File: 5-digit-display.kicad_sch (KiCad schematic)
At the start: 6 parts, among them U13 MAX7219, U14 3_digit_7_segment_display, U15 2_digit_7_segment_display

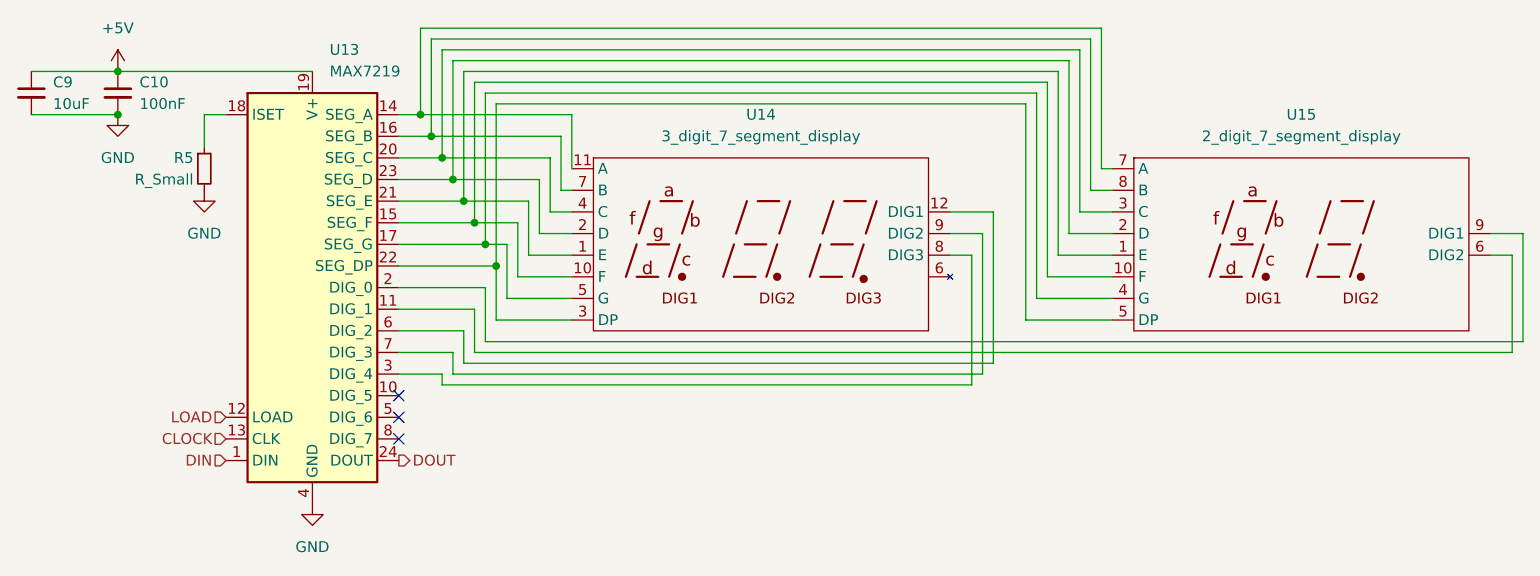
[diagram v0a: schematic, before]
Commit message: Add RP2040
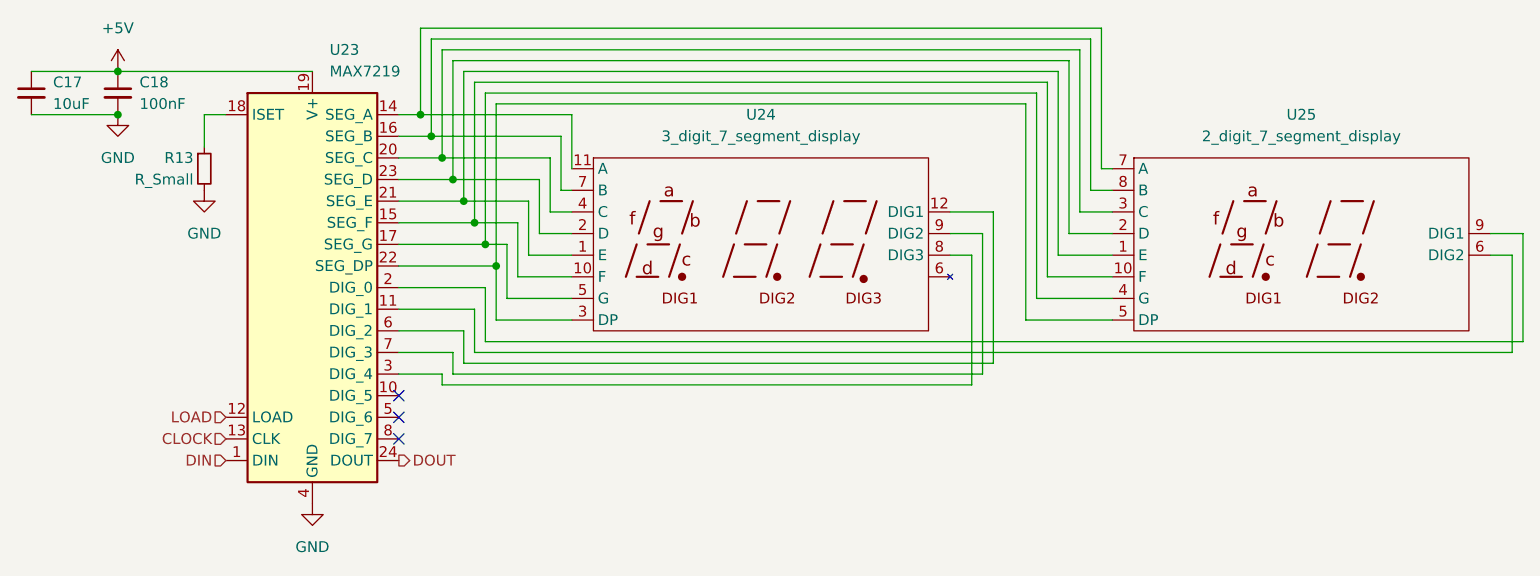
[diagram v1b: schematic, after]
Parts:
- renumbered C9 to C17, C10 to C18, R5 to R13, U13 to U23, U14 to U24, U15 to U25
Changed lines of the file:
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@@
   (symbol (lib_id "power:GND") (at 64.77 92.71 0)
     (in_bom yes) (on_board yes) (fields_autoplaced)
-    (property "Reference" "#PWR031" (id 0) (at 64.77 99.06 0)
+    (property "Reference" "#PWR040" (id 0) (at 64.77 99.06 0)
       (effects (font (size 1.27 1.27)) hide)
     )
@@
   (symbol (lib_id "Device:C_Small") (at 54.61 81.28 0)
     (in_bom yes) (on_board yes) (fields_autoplaced)
-    (property "Reference" "C10" (id 0) (at 57.15 80.0162 0)
+    (property "Reference" "C18" (id 0) (at 57.15 80.0162 0)
       (effects (font (size 1.27 1.27)) (justify left))
     )
@@
   (symbol (lib_id "Device:R_Small") (at 64.77 90.17 0)
     (in_bom yes) (on_board yes)
-    (property "Reference" "R5" (id 0) (at 63.5 88.9 0)
+    (property "Reference" "R13" (id 0) (at 63.5 88.9 0)
       (effects (font (size 1.27 1.27)) (justify right))
     )
@@
   (symbol (lib_id "Generic-radio-stack:2_digit_7_segment_display") (at 193.04 99.06 0)
     (in_bom yes) (on_board yes) (fields_autoplaced)
-    (property "Reference" "U15" (id 0) (at 193.675 83.82 0))
+    (property "Reference" "U25" (id 0) (at 193.675 83.82 0))
     (property "Value" "2_digit_7_segment_display" (id 1) (at 193.675 86.36 0))
     (property "Footprint" "" (id 2) (at 203.2 99.06 0)
@@
   (symbol (lib_id "power:GND") (at 77.47 129.54 0)
     (in_bom yes) (on_board yes) (fields_autoplaced)
-    (property "Reference" "#PWR032" (id 0) (at 77.47 135.89 0)
+    (property "Reference" "#PWR041" (id 0) (at 77.47 135.89 0)
       (effects (font (size 1.27 1.27)) hide)
     )
@@
   (symbol (lib_id "Driver_LED:MAX7219") (at 77.47 104.14 0)
     (in_bom yes) (on_board yes) (fields_autoplaced)
-    (property "Reference" "U13" (id 0) (at 79.4894 76.2 0)
+    (property "Reference" "U23" (id 0) (at 79.4894 76.2 0)
       (effects (font (size 1.27 1.27)) (justify left))
     )
@@
   (symbol (lib_id "Generic-radio-stack:3_digit_7_segment_display") (at 129.54 99.06 0)
     (in_bom yes) (on_board yes) (fields_autoplaced)
-    (property "Reference" "U14" (id 0) (at 130.175 83.82 0))
+    (property "Reference" "U24" (id 0) (at 130.175 83.82 0))
     (property "Value" "3_digit_7_segment_display" (id 1) (at 130.175 86.36 0))
     (property "Footprint" "" (id 2) (at 134.62 99.06 0)
@@
   (symbol (lib_id "power:GND") (at 54.61 83.82 0)
     (in_bom yes) (on_board yes) (fields_autoplaced)
-    (property "Reference" "#PWR030" (id 0) (at 54.61 90.17 0)
+    (property "Reference" "#PWR039" (id 0) (at 54.61 90.17 0)
       (effects (font (size 1.27 1.27)) hide)
     )
@@
   (symbol (lib_id "power:+5V") (at 54.61 78.74 0)
     (in_bom yes) (on_board yes) (fields_autoplaced)
-    (property "Reference" "#PWR029" (id 0) (at 54.61 82.55 0)
+    (property "Reference" "#PWR038" (id 0) (at 54.61 82.55 0)
       (effects (font (size 1.27 1.27)) hide)
     )
@@
   (symbol (lib_id "Device:C_Small") (at 44.45 81.28 0)
     (in_bom yes) (on_board yes) (fields_autoplaced)
-    (property "Reference" "C9" (id 0) (at 46.99 80.0162 0)
+    (property "Reference" "C17" (id 0) (at 46.99 80.0162 0)
       (effects (font (size 1.27 1.27)) (justify left))
     )

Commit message: Bunch more schematic work
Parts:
- C18: footprint (none) -> Capacitor_SMD:C_0805_2012Metric
- R17: renamed from R13; footprint (none) -> Resistor_SMD:R_0805_2012Metric
- U23: footprint (none) -> Package_SO:SOIC-24W_7.5x15.4mm_P1.27mm
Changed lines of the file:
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@@
   (symbol (lib_id "power:GND") (at 64.77 92.71 0)
     (in_bom yes) (on_board yes) (fields_autoplaced)
-    (property "Reference" "#PWR040" (id 0) (at 64.77 99.06 0)
+    (property "Reference" "#PWR042" (id 0) (at 64.77 99.06 0)
       (effects (font (size 1.27 1.27)) hide)
     )
@@
       (effects (font (size 1.27 1.27)) (justify left))
     )
-    (property "Footprint" "" (id 2) (at 54.61 81.28 0)
+    (property "Footprint" "Capacitor_SMD:C_0805_2012Metric" (id 2) (at 54.61 81.28 0)
       (effects (font (size 1.27 1.27)) hide)
     )
@@
   (symbol (lib_id "Device:R_Small") (at 64.77 90.17 0)
     (in_bom yes) (on_board yes)
-    (property "Reference" "R13" (id 0) (at 63.5 88.9 0)
+    (property "Reference" "R17" (id 0) (at 63.5 88.9 0)
       (effects (font (size 1.27 1.27)) (justify right))
     )
@@
       (effects (font (size 1.27 1.27)) (justify right))
     )
-    (property "Footprint" "" (id 2) (at 64.77 90.17 0)
+    (property "Footprint" "Resistor_SMD:R_0805_2012Metric" (id 2) (at 64.77 90.17 0)
       (effects (font (size 1.27 1.27)) hide)
     )
@@
   (symbol (lib_id "power:GND") (at 77.47 129.54 0)
     (in_bom yes) (on_board yes) (fields_autoplaced)
-    (property "Reference" "#PWR041" (id 0) (at 77.47 135.89 0)
+    (property "Reference" "#PWR043" (id 0) (at 77.47 135.89 0)
       (effects (font (size 1.27 1.27)) hide)
     )
@@
       (effects (font (size 1.27 1.27)) (justify left))
     )
-    (property "Footprint" "" (id 2) (at 76.2 102.87 0)
+    (property "Footprint" "Package_SO:SOIC-24W_7.5x15.4mm_P1.27mm" (id 2) (at 76.2 102.87 0)
       (effects (font (size 1.27 1.27)) hide)
     )
@@
   (symbol (lib_id "power:GND") (at 54.61 83.82 0)
     (in_bom yes) (on_board yes) (fields_autoplaced)
-    (property "Reference" "#PWR039" (id 0) (at 54.61 90.17 0)
+    (property "Reference" "#PWR041" (id 0) (at 54.61 90.17 0)
       (effects (font (size 1.27 1.27)) hide)
     )
@@
   (symbol (lib_id "power:+5V") (at 54.61 78.74 0)
     (in_bom yes) (on_board yes) (fields_autoplaced)
-    (property "Reference" "#PWR038" (id 0) (at 54.61 82.55 0)
+    (property "Reference" "#PWR040" (id 0) (at 54.61 82.55 0)
       (effects (font (size 1.27 1.27)) hide)
     )

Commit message: Add display footprints and models
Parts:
- C17: footprint (none) -> Generic-radio-stack:Perfect_0402
- C18: footprint Capacitor_SMD:C_0805_2012Metric -> Generic-radio-stack:Perfect_0402
- R17: footprint Resistor_SMD:R_0805_2012Metric -> Generic-radio-stack:Perfect_0402
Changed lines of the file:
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@@
       (effects (font (size 1.27 1.27)) (justify left))
     )
-    (property "Footprint" "Capacitor_SMD:C_0805_2012Metric" (id 2) (at 54.61 81.28 0)
+    (property "Footprint" "Generic-radio-stack:Perfect_0402" (id 2) (at 54.61 81.28 0)
       (effects (font (size 1.27 1.27)) hide)
     )
@@
       (effects (font (size 1.27 1.27)) (justify right))
     )
-    (property "Footprint" "Resistor_SMD:R_0805_2012Metric" (id 2) (at 64.77 90.17 0)
+    (property "Footprint" "Generic-radio-stack:Perfect_0402" (id 2) (at 64.77 90.17 0)
       (effects (font (size 1.27 1.27)) hide)
     )
@@
       (effects (font (size 1.27 1.27)) (justify left))
     )
-    (property "Footprint" "" (id 2) (at 44.45 81.28 0)
+    (property "Footprint" "Generic-radio-stack:Perfect_0402" (id 2) (at 44.45 81.28 0)
       (effects (font (size 1.27 1.27)) hide)
     )

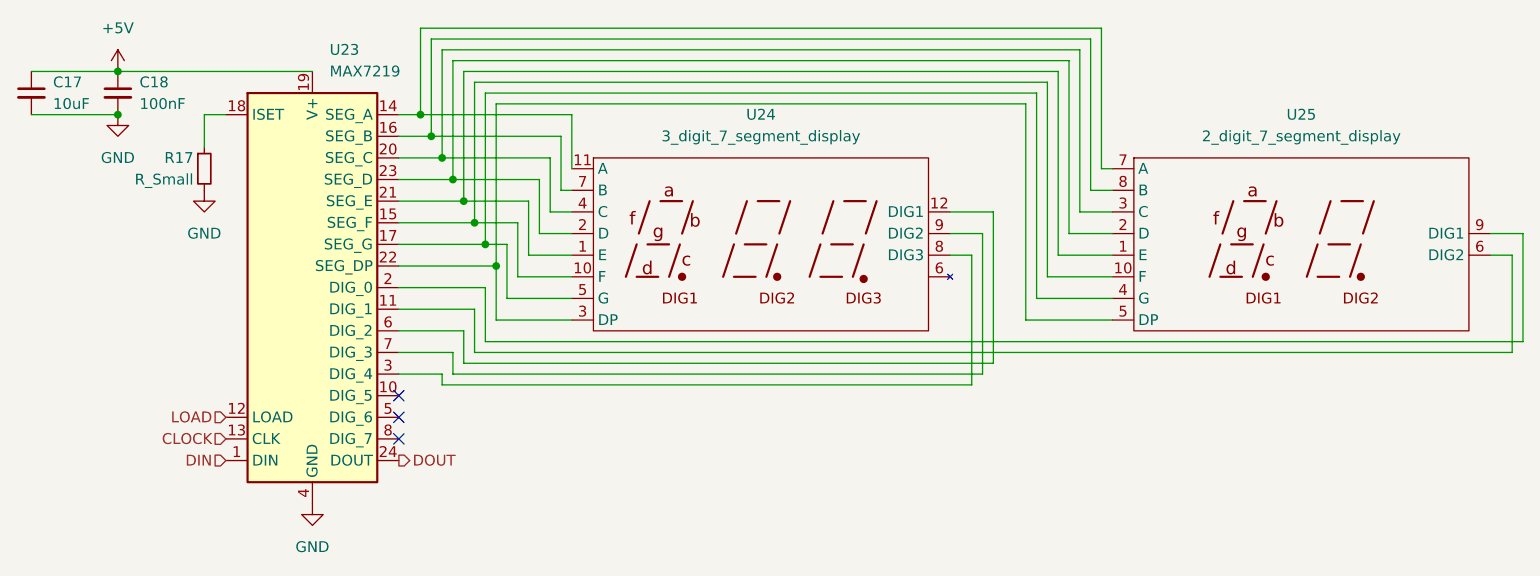
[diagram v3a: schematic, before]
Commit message: Custom component for six digit display
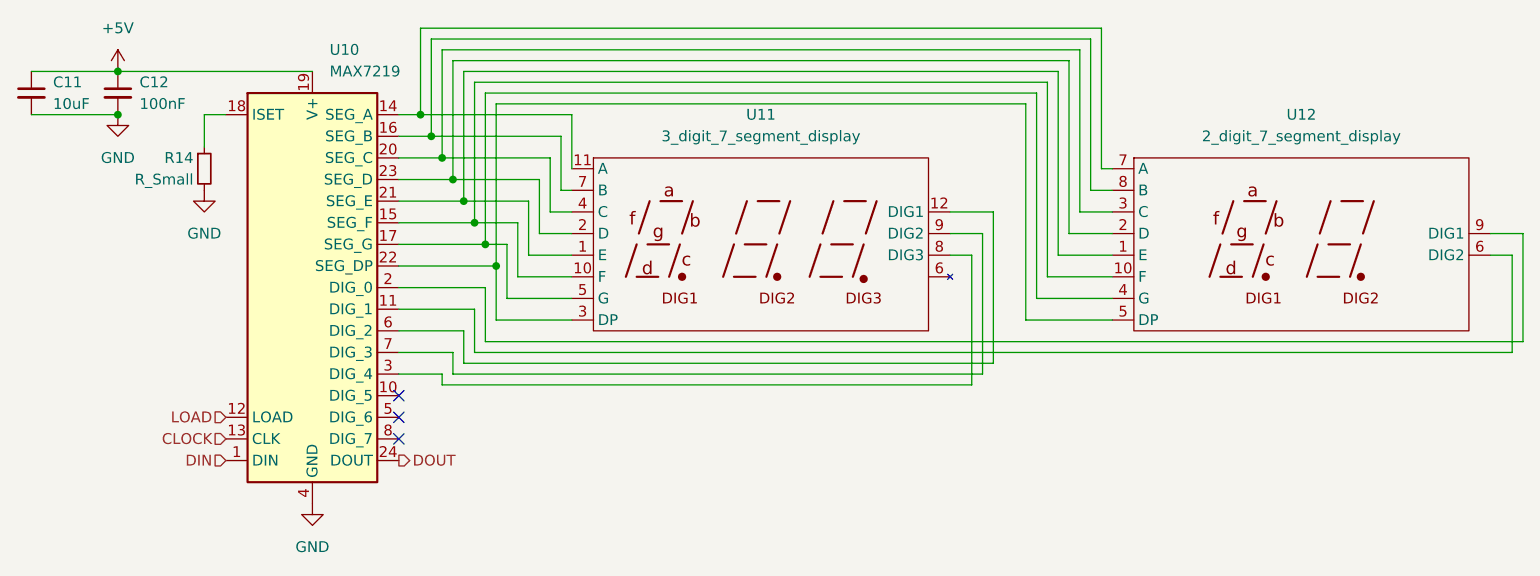
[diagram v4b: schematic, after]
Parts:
- U11: renamed from U24; footprint (none) -> Generic-radio-stack:3_digit_7_segment_LED
- U12: renamed from U25; footprint (none) -> Generic-radio-stack:2_digit_7_segment_LED
- renumbered C17 to C11, C18 to C12, R17 to R14, U23 to U10
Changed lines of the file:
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@@
   (symbol (lib_id "Device:C_Small") (at 54.61 81.28 0)
     (in_bom yes) (on_board yes) (fields_autoplaced)
-    (property "Reference" "C18" (id 0) (at 57.15 80.0162 0)
+    (property "Reference" "C12" (id 0) (at 57.15 80.0162 0)
       (effects (font (size 1.27 1.27)) (justify left))
     )
@@
   (symbol (lib_id "Device:R_Small") (at 64.77 90.17 0)
     (in_bom yes) (on_board yes)
-    (property "Reference" "R17" (id 0) (at 63.5 88.9 0)
+    (property "Reference" "R14" (id 0) (at 63.5 88.9 0)
       (effects (font (size 1.27 1.27)) (justify right))
     )
@@
   (symbol (lib_id "Generic-radio-stack:2_digit_7_segment_display") (at 193.04 99.06 0)
     (in_bom yes) (on_board yes) (fields_autoplaced)
-    (property "Reference" "U25" (id 0) (at 193.675 83.82 0))
+    (property "Reference" "U12" (id 0) (at 193.675 83.82 0))
     (property "Value" "2_digit_7_segment_display" (id 1) (at 193.675 86.36 0))
-    (property "Footprint" "" (id 2) (at 203.2 99.06 0)
+    (property "Footprint" "Generic-radio-stack:2_digit_7_segment_LED" (id 2) (at 203.2 99.06 0)
       (effects (font (size 1.27 1.27)) hide)
     )
@@
   (symbol (lib_id "Driver_LED:MAX7219") (at 77.47 104.14 0)
     (in_bom yes) (on_board yes) (fields_autoplaced)
-    (property "Reference" "U23" (id 0) (at 79.4894 76.2 0)
+    (property "Reference" "U10" (id 0) (at 79.4894 76.2 0)
       (effects (font (size 1.27 1.27)) (justify left))
     )
@@
   (symbol (lib_id "Generic-radio-stack:3_digit_7_segment_display") (at 129.54 99.06 0)
     (in_bom yes) (on_board yes) (fields_autoplaced)
-    (property "Reference" "U24" (id 0) (at 130.175 83.82 0))
+    (property "Reference" "U11" (id 0) (at 130.175 83.82 0))
     (property "Value" "3_digit_7_segment_display" (id 1) (at 130.175 86.36 0))
-    (property "Footprint" "" (id 2) (at 134.62 99.06 0)
+    (property "Footprint" "Generic-radio-stack:3_digit_7_segment_LED" (id 2) (at 134.62 99.06 0)
       (effects (font (size 1.27 1.27)) hide)
     )
@@
   (symbol (lib_id "Device:C_Small") (at 44.45 81.28 0)
     (in_bom yes) (on_board yes) (fields_autoplaced)
-    (property "Reference" "C17" (id 0) (at 46.99 80.0162 0)
+    (property "Reference" "C11" (id 0) (at 46.99 80.0162 0)
       (effects (font (size 1.27 1.27)) (justify left))
     )

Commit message: More footprint updates
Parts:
- removed U11: 3_digit_7_segment_display, Generic-radio-stack:3_digit_7_segment_LED, symbol Generic-radio-stack:3_digit_7_segment_display
- removed U12: 2_digit_7_segment_display, Generic-radio-stack:2_digit_7_segment_LED, symbol Generic-radio-stack:2_digit_7_segment_display
- added U11: 5_digit_7_segment_display, Generic-radio-stack:5 digit (3+2) 7 segment LED display, symbol Generic-radio-stack:5_digit_7_segment_display
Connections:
- net E: now reaches U10.21 (SEG_E)
- net E: now also U11.1 (E), U11.13 (E')
- net F: now reaches U10.15 (SEG_F)
- net F: now also U11.10 (F), U11.22 (F')
- net D: now reaches U10.23 (SEG_D)
- net D: now also U11.14 (D'), U11.2 (D)
- net C: now reaches U10.20 (SEG_C)
- net C: now also U11.15 (C'), U11.4 (C)
- net G: now reaches U10.17 (SEG_G)
- net G: now also U11.16 (G'), U11.5 (G)
- net DP: now reaches U10.22 (SEG_DP)
- net DP: now also U11.17 (DP'), U11.3 (DP)
- net DIG_1: now reaches U10.11 (DIG_1)
- net DIG_1: now also U11.21 (DIG1')
- net A: now reaches U10.14 (SEG_A)
- net A: now also U11.11 (A), U11.19 (A')
- net B: now reaches U10.16 (SEG_B)
- net B: now also U11.20 (B'), U11.7 (B)
- net DIG_0: now reaches U10.2 (DIG_0)
- net DIG_0: now also U11.18 (DIG2')
- net DIG_4: now reaches U10.3 (DIG_4)
- net DIG_4: now also U11.12 (DIG1)
- net DIG_2: now reaches U10.6 (DIG_2)
- net DIG_2: now also U11.8 (DIG3)
- net DIG_3: now reaches U10.7 (DIG_3)
- net DIG_3: now also U11.9 (DIG2)

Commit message: Board layout begins. Ugh.
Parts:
- renumbered C11 to C17, C12 to C18, R14 to R17, U10 to U16, U11 to U17
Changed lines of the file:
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@@
   (symbol (lib_id "power:GND") (at 64.77 92.71 0)
     (in_bom yes) (on_board yes) (fields_autoplaced)
-    (property "Reference" "#PWR030" (id 0) (at 64.77 99.06 0)
+    (property "Reference" "#PWR042" (id 0) (at 64.77 99.06 0)
       (effects (font (size 1.27 1.27)) hide)
     )
@@
   (symbol (lib_id "Device:C_Small") (at 54.61 81.28 0)
     (in_bom yes) (on_board yes) (fields_autoplaced)
-    (property "Reference" "C12" (id 0) (at 57.15 80.0162 0)
+    (property "Reference" "C18" (id 0) (at 57.15 80.0162 0)
       (effects (font (size 1.27 1.27)) (justify left))
     )
@@
   (symbol (lib_id "Device:R_Small") (at 64.77 90.17 0)
     (in_bom yes) (on_board yes)
-    (property "Reference" "R14" (id 0) (at 63.5 88.9 0)
+    (property "Reference" "R17" (id 0) (at 63.5 88.9 0)
       (effects (font (size 1.27 1.27)) (justify right))
     )
@@
   (symbol (lib_id "power:GND") (at 77.47 129.54 0)
     (in_bom yes) (on_board yes) (fields_autoplaced)
-    (property "Reference" "#PWR031" (id 0) (at 77.47 135.89 0)
+    (property "Reference" "#PWR043" (id 0) (at 77.47 135.89 0)
       (effects (font (size 1.27 1.27)) hide)
     )
@@
   (symbol (lib_id "Driver_LED:MAX7219") (at 77.47 104.14 0)
     (in_bom yes) (on_board yes) (fields_autoplaced)
-    (property "Reference" "U10" (id 0) (at 79.4894 76.2 0)
+    (property "Reference" "U16" (id 0) (at 79.4894 76.2 0)
       (effects (font (size 1.27 1.27)) (justify left))
     )
@@
   (symbol (lib_id "power:GND") (at 54.61 83.82 0)
     (in_bom yes) (on_board yes) (fields_autoplaced)
-    (property "Reference" "#PWR029" (id 0) (at 54.61 90.17 0)
+    (property "Reference" "#PWR041" (id 0) (at 54.61 90.17 0)
       (effects (font (size 1.27 1.27)) hide)
     )
@@
   (symbol (lib_id "power:+5V") (at 54.61 78.74 0)
     (in_bom yes) (on_board yes) (fields_autoplaced)
-    (property "Reference" "#PWR028" (id 0) (at 54.61 82.55 0)
+    (property "Reference" "#PWR040" (id 0) (at 54.61 82.55 0)
       (effects (font (size 1.27 1.27)) hide)
     )
@@
   (symbol (lib_id "Generic-radio-stack:5_digit_7_segment_display") (at 129.54 92.71 0)
     (in_bom yes) (on_board yes) (fields_autoplaced)
-    (property "Reference" "U11" (id 0) (at 129.54 77.47 0))
+    (property "Reference" "U17" (id 0) (at 129.54 77.47 0))
     (property "Value" "5_digit_7_segment_display" (id 1) (at 129.54 80.01 0))
     (property "Footprint" "Generic-radio-stack:5 digit (3+2) 7 segment LED display" (id 2) (at 129.54 106.68 0)
@@
   (symbol (lib_id "Device:C_Small") (at 44.45 81.28 0)
     (in_bom yes) (on_board yes) (fields_autoplaced)
-    (property "Reference" "C11" (id 0) (at 46.99 80.0162 0)
+    (property "Reference" "C17" (id 0) (at 46.99 80.0162 0)
       (effects (font (size 1.27 1.27)) (justify left))
     )
